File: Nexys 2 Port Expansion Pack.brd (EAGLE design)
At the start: 58.4 x 84.8 mm, 24 parts, among them IC1 74HC245N, IC2 74HC245N, IC3 74HC245N

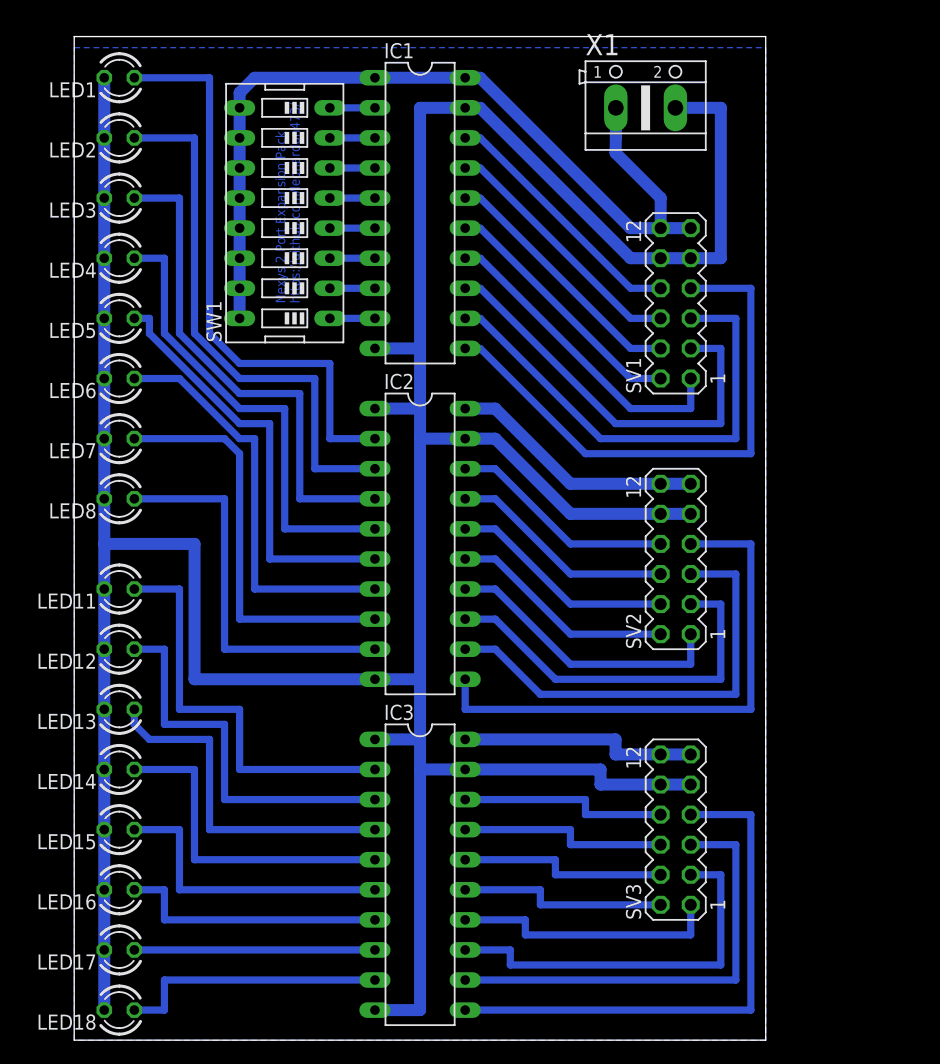
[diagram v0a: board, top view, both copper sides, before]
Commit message: Add resistence to the dipswitch
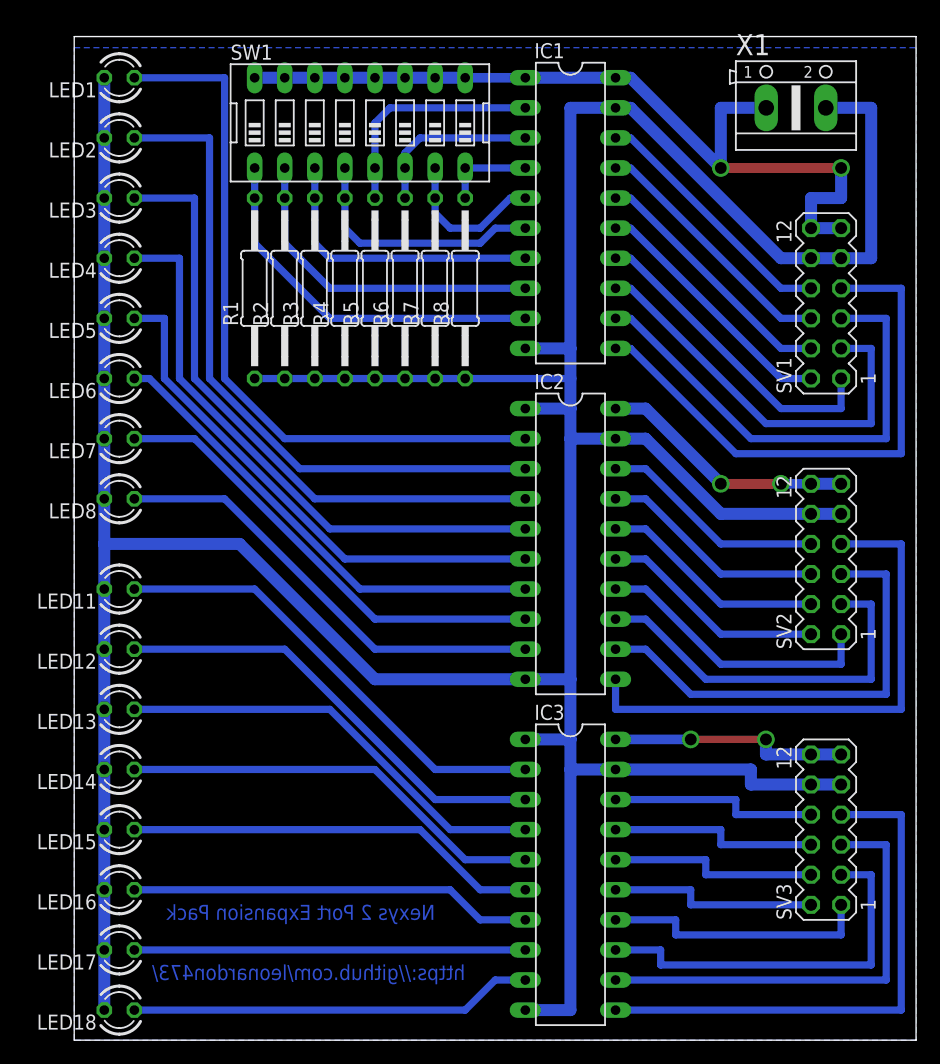
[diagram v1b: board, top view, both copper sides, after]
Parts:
- added R1, R2, R3, R4, R5, R6, R7, R8: (no value), resistor:0207/15
- moved SV1 12.7 mm to (63.5, 62.2)
- moved SV2 12.7 mm to (63.5, 40.6)
- moved SV3 12.7 mm to (63.5, 17.8)
- moved X1 12.7 mm to (61.0, 78.7)
- moved IC1 12.7 mm to (41.9, 69.8)
- moved IC2 12.7 mm to (41.9, 41.9)
- moved IC3 12.7 mm to (41.9, 14.0)
- moved SW1 9.92 mm to (24.1, 77.5), turned to 0 degrees
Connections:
- removed net N$1: IC1.2, SW1.8
- removed net N$2: IC1.3, SW1.7
- removed net N$3: IC1.4, SW1.6
- removed net N$4: IC1.5, SW1.5
- removed net N$5: IC1.6, SW1.4
- removed net N$6: IC1.7, SW1.3
- removed net N$7: IC1.8, SW1.2
- removed net N$8: IC1.9, SW1.1
- new net A11: IC1.2, R5.2, SW1.5
- new net A21: IC1.3, R6.2, SW1.6
- new net A31: IC1.4, R8.2, SW1.8
- new net A41: IC1.5, R7.2, SW1.7
- new net A51: IC1.6, R4.2, SW1.4
- new net A61: IC1.7, R3.2, SW1.3
- new net A71: IC1.8, R2.2, SW1.2
- new net A81: IC1.9, R1.2, SW1.1
- net GND: now also R1.1, R2.1, R3.1, R4.1, R5.1, R6.1, R7.1, R8.1
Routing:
- net GND: track 307.6 -> 340.3 mm
- net A81: track 0.00 -> 31.8 mm
- net A71: track 0.00 -> 28.2 mm
- net A61: track 0.00 -> 24.7 mm
- net A51: track 0.00 -> 21.4 mm
- net A11: track 0.00 -> 19.6 mm
- net A21: track 0.00 -> 14.5 mm
- net A41: track 0.00 -> 13.0 mm
- net N$35: track 20.3 -> 33.0 mm
- net N$34: track 22.9 -> 34.1 mm
- net N$36: track 22.9 -> 34.1 mm
- net N$12: track 49.3 -> 60.5 mm
- net N$22: track 46.0 -> 56.5 mm
- net N$33: track 25.4 -> 35.1 mm
- net N$24: track 42.7 -> 52.5 mm
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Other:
- board size 58.4 x 84.8 mm -> 71.1 x 84.8 mm
- board text added: "Nexys 2 Port Expansion Pack"
- board text added: "https://github.com/leonardon473/"
- board text removed: "Nexys 2 Port Expansion Pack https://github.com/leonardon473/"

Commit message: Separate the tracks
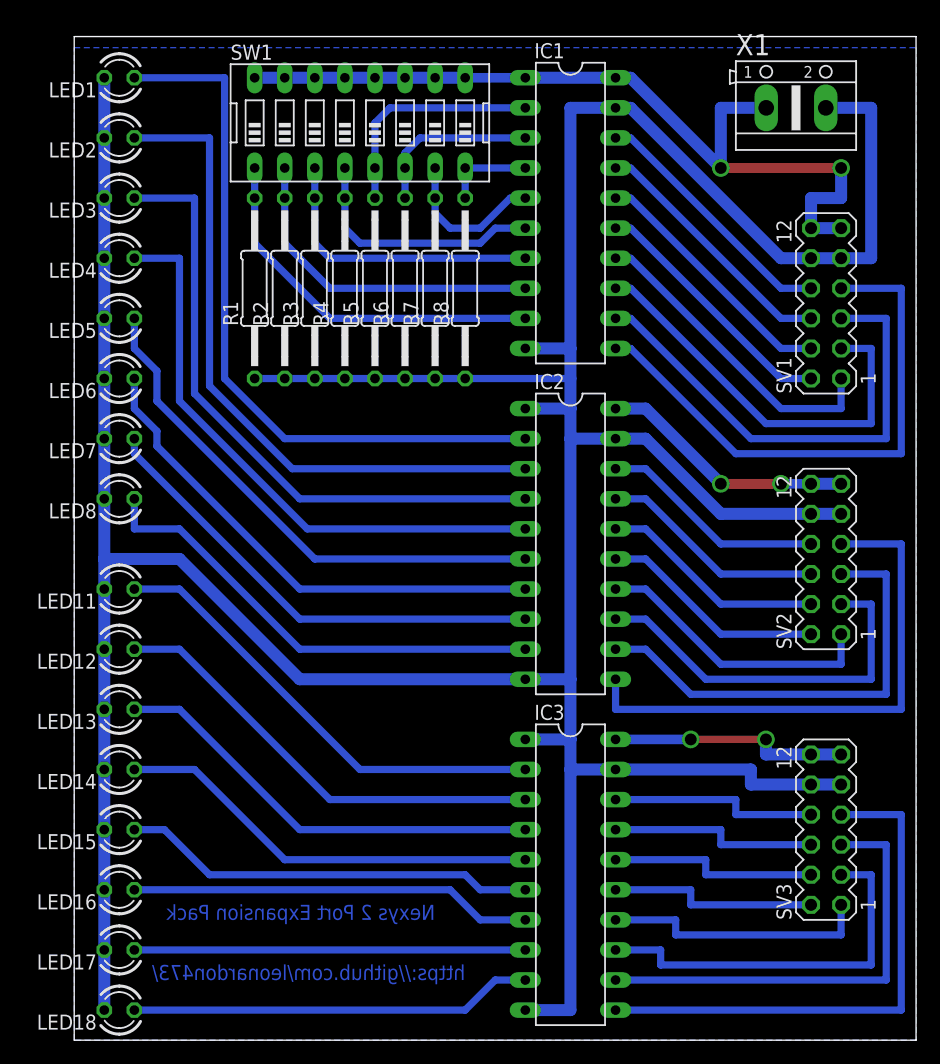
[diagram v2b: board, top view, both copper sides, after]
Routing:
- net N$27: track 40.4 -> 42.6 mm
- net N$29: track 38.3 -> 39.8 mm
- net N$25: track 48.4 -> 49.6 mm
- net N$24: track 52.5 -> 53.2 mm
- net N$28: track 39.3 -> 40.1 mm
- net GND: track 340.3 -> 339.8 mm
